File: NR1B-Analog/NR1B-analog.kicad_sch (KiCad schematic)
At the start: 73 parts, among them J8 UART, U1 DAC11001BPFBR, U10 LT3042MPMSE-PBF, U11 LDK320ADU120R, U12 20K, U13 OPA2189IDR, U14 DAC11001BPFBR, U2 ADR444ARZ, U3 OPA189IDGKT, U4 OPA2189IDR, U6 OPA2189IDR, U7 LT3093EMSE-PBF, U8 20K, U9 10K

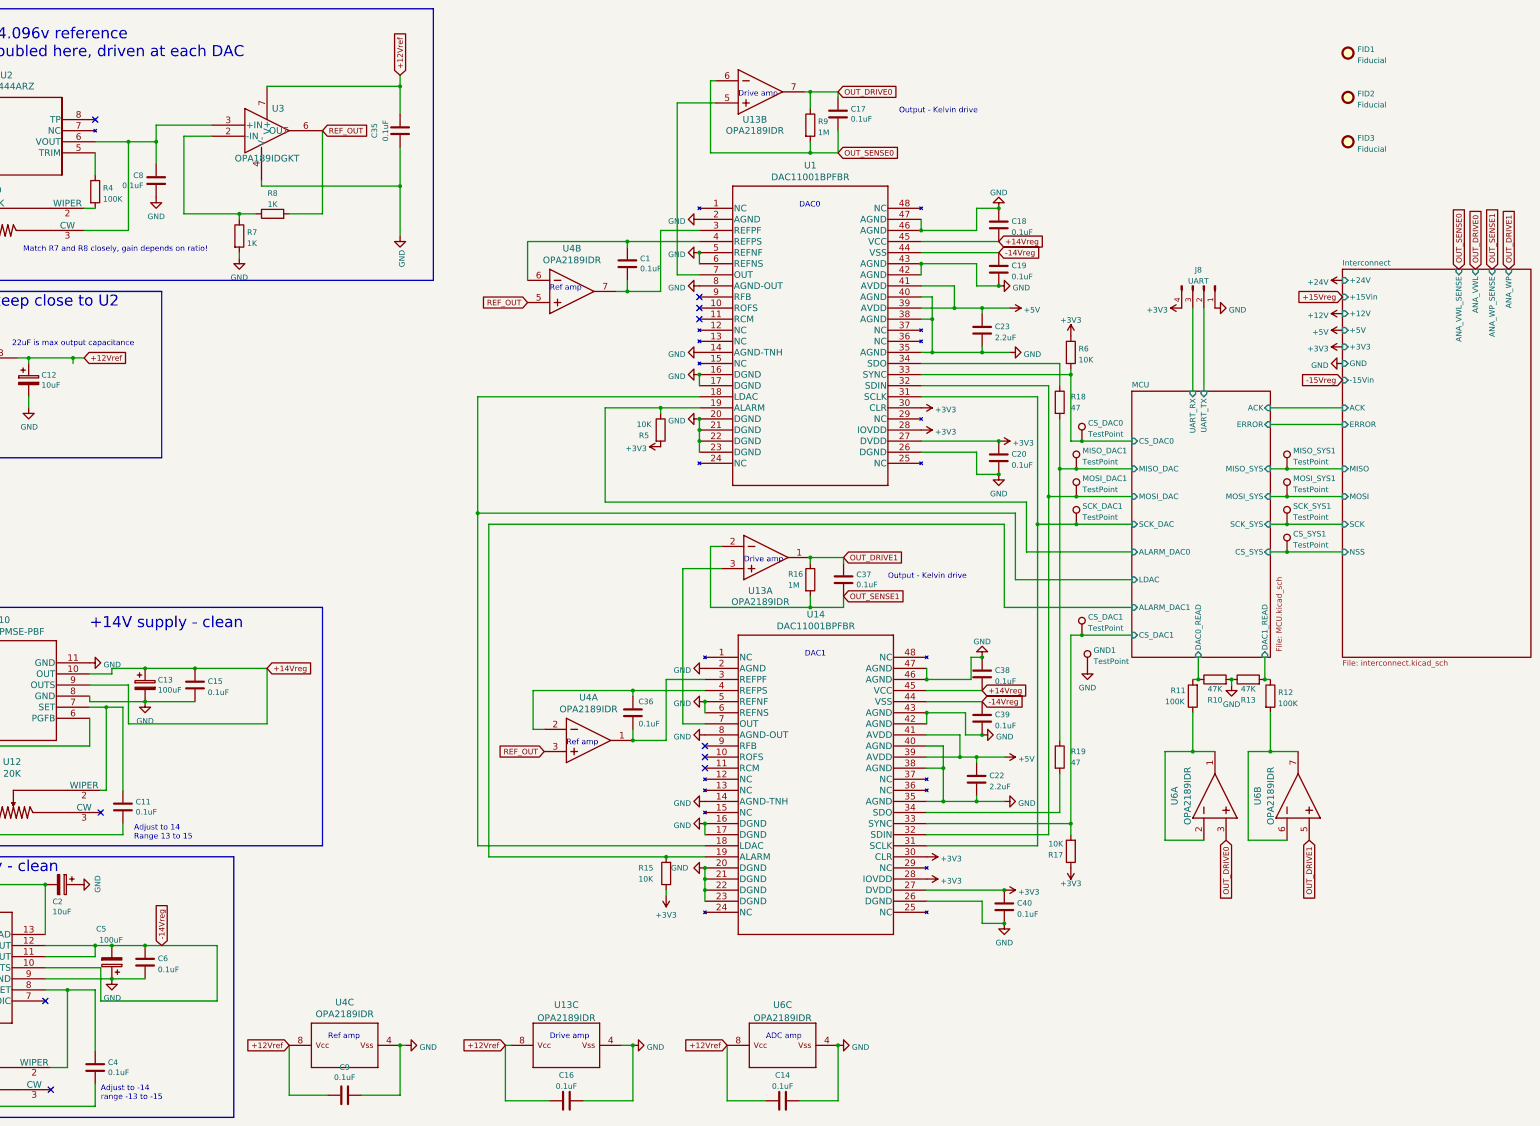
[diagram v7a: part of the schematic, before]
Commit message: Changed footprints, re-routed
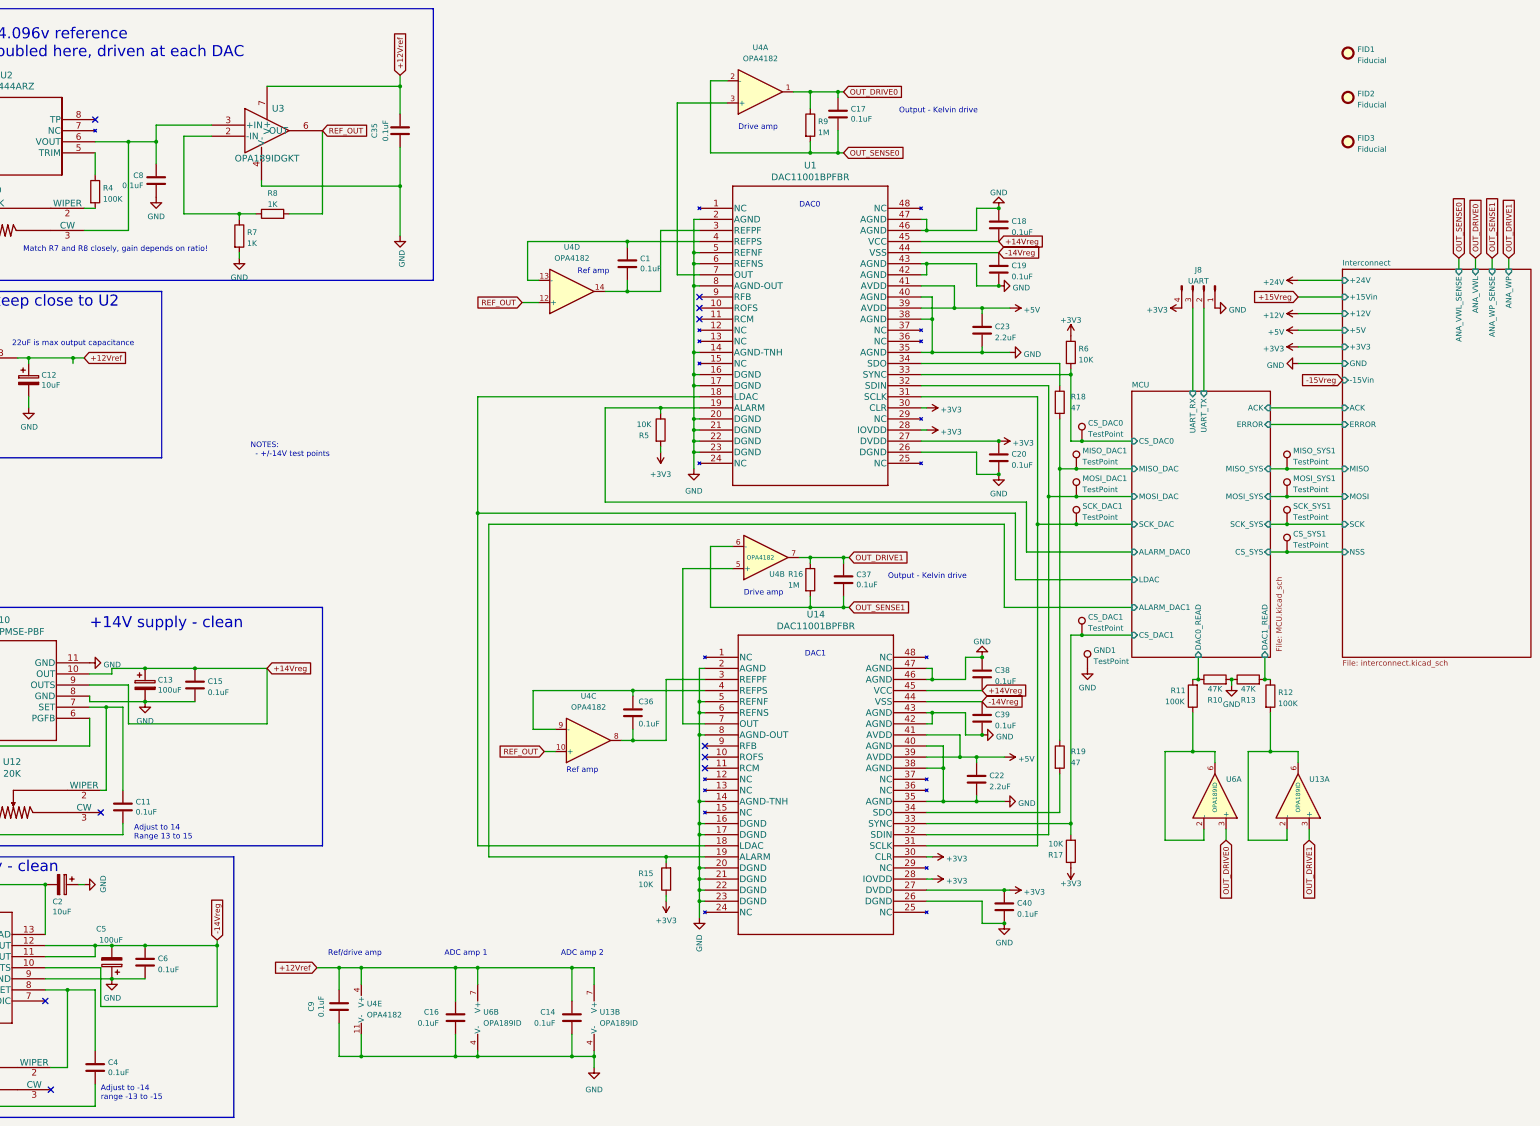
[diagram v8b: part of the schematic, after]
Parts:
- removed U13, U4, U6: OPA2189IDR, Package_SO:VSSOP-8_3.0x3.0mm_P0.65mm, symbol 2022-06-28_19-20-58:OPA2189IDR
- added U13, U6: OPA189ID, Package_SO:SOIC-8_3.9x4.9mm_P1.27mm, symbol NISoC-Socket:OPA189ID
- added U4: OPA4182, Package_SO:SOIC-14_3.9x8.7mm_P1.27mm, symbol NISoC-Socket:OPA4182
- U3: footprint Package_SO:VSSOP-8_3.0x3.0mm_P0.65mm -> Package_SO:SOIC-8_3.9x4.9mm_P1.27mm
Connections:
- net +12Vref: now also C14.2, C16.2, C9.2, U13.7 (V+), U4.4 (V+), U6.7 (V+); no longer C14.1, C16.1, C9.1
- net GND: now also C14.1, C16.1, C9.1, U13.4 (V-), U4.11 (V-), U6.4 (V-); no longer C14.2, C16.2, C9.2
- net OUT_DRIVE0: now also U4.1, U6.3 (+)
- net OUT_DRIVE1: now also U13.3 (+), U4.7
- net OUT_SENSE0: now also U4.2 (-)
- net OUT_SENSE1: now also U4.6 (-)
- net REF_OUT: now also U4.10 (+), U4.12 (+)
- net at C1.2, U1.3 (REFPF): now also U4.14
- net at C1.1, U1.4 (REFPS): now also U4.13 (-)
- net at U1.7 (OUT): now also U4.3 (+)
- net at C36.2, U14.3 (REFPF): now also U4.8
- net at C36.1, U14.4 (REFPS): now also U4.9 (-)
- net at R11.1: now also U6.2 (-), U6.6
- net at U14.7 (OUT): now also U4.5 (+)
- net at R12.2: now also U13.2 (-), U13.6
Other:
- note added: "ADC amp 1"
- note added: "ADC amp 2"
- note added: "NOTES: - +/-14V test points"
- note added: "Ref/drive amp"
- note removed: "ADC amp"
- moved on the sheet: C14, C16, C9, R15
